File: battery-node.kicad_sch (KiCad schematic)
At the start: 16 parts, among them Q2 TK11S10N1L,LQ, U1 L99BM114-TR

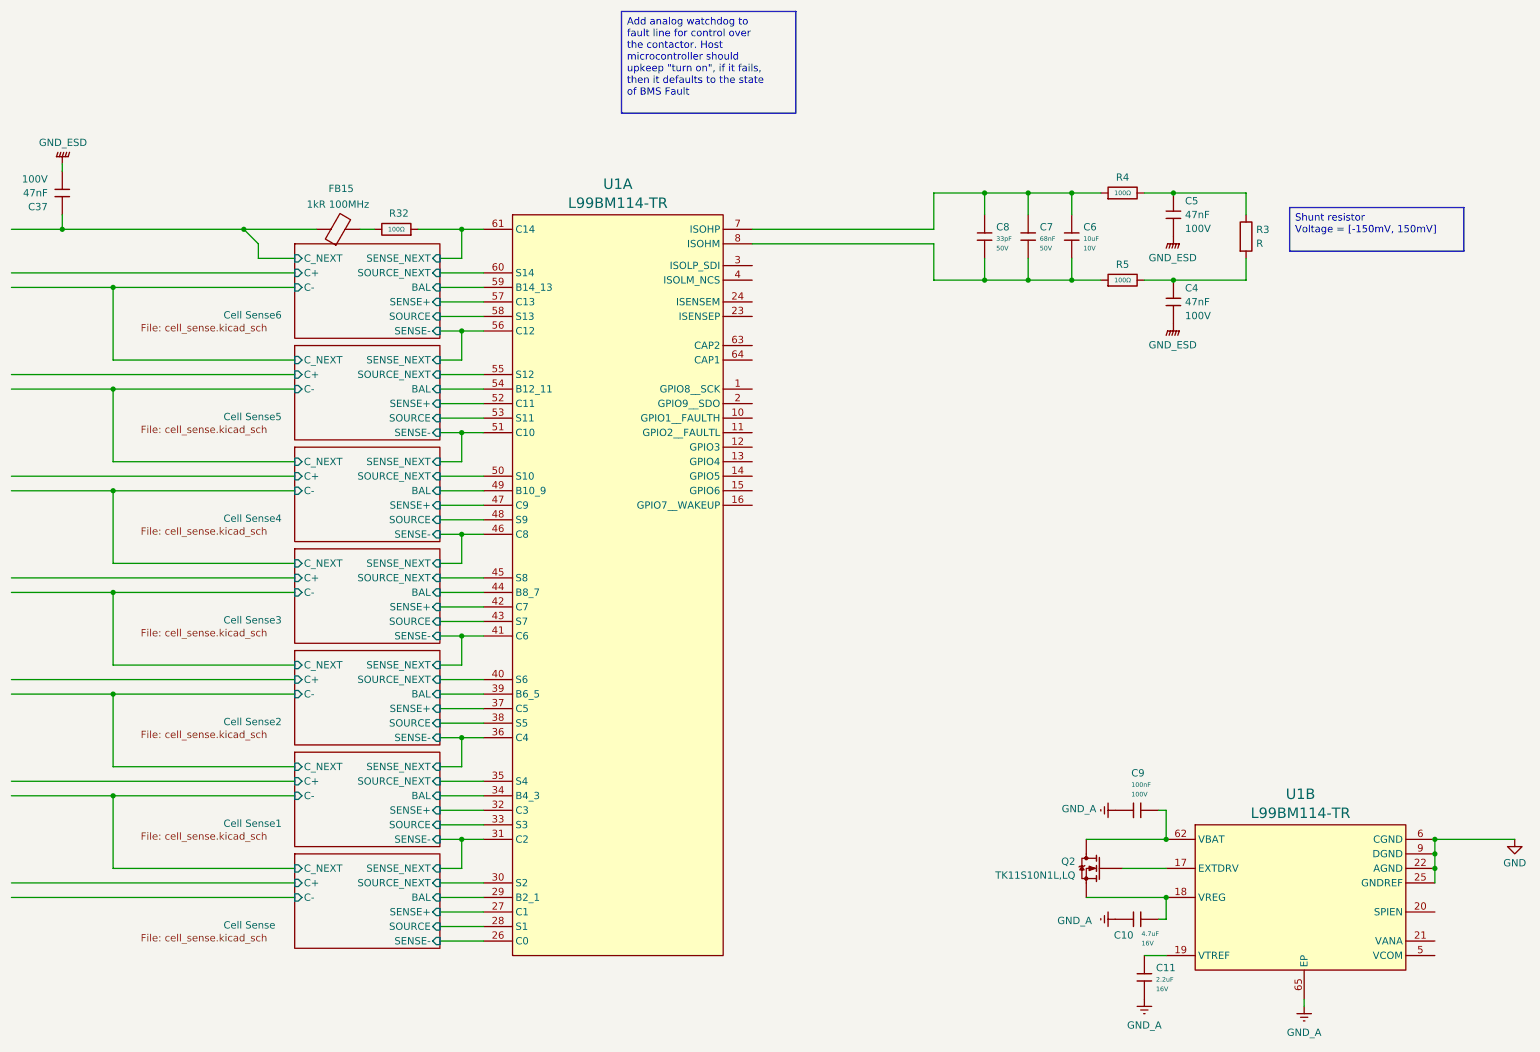
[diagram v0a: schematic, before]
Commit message: Continued work on adding subcircuits for L99BM114
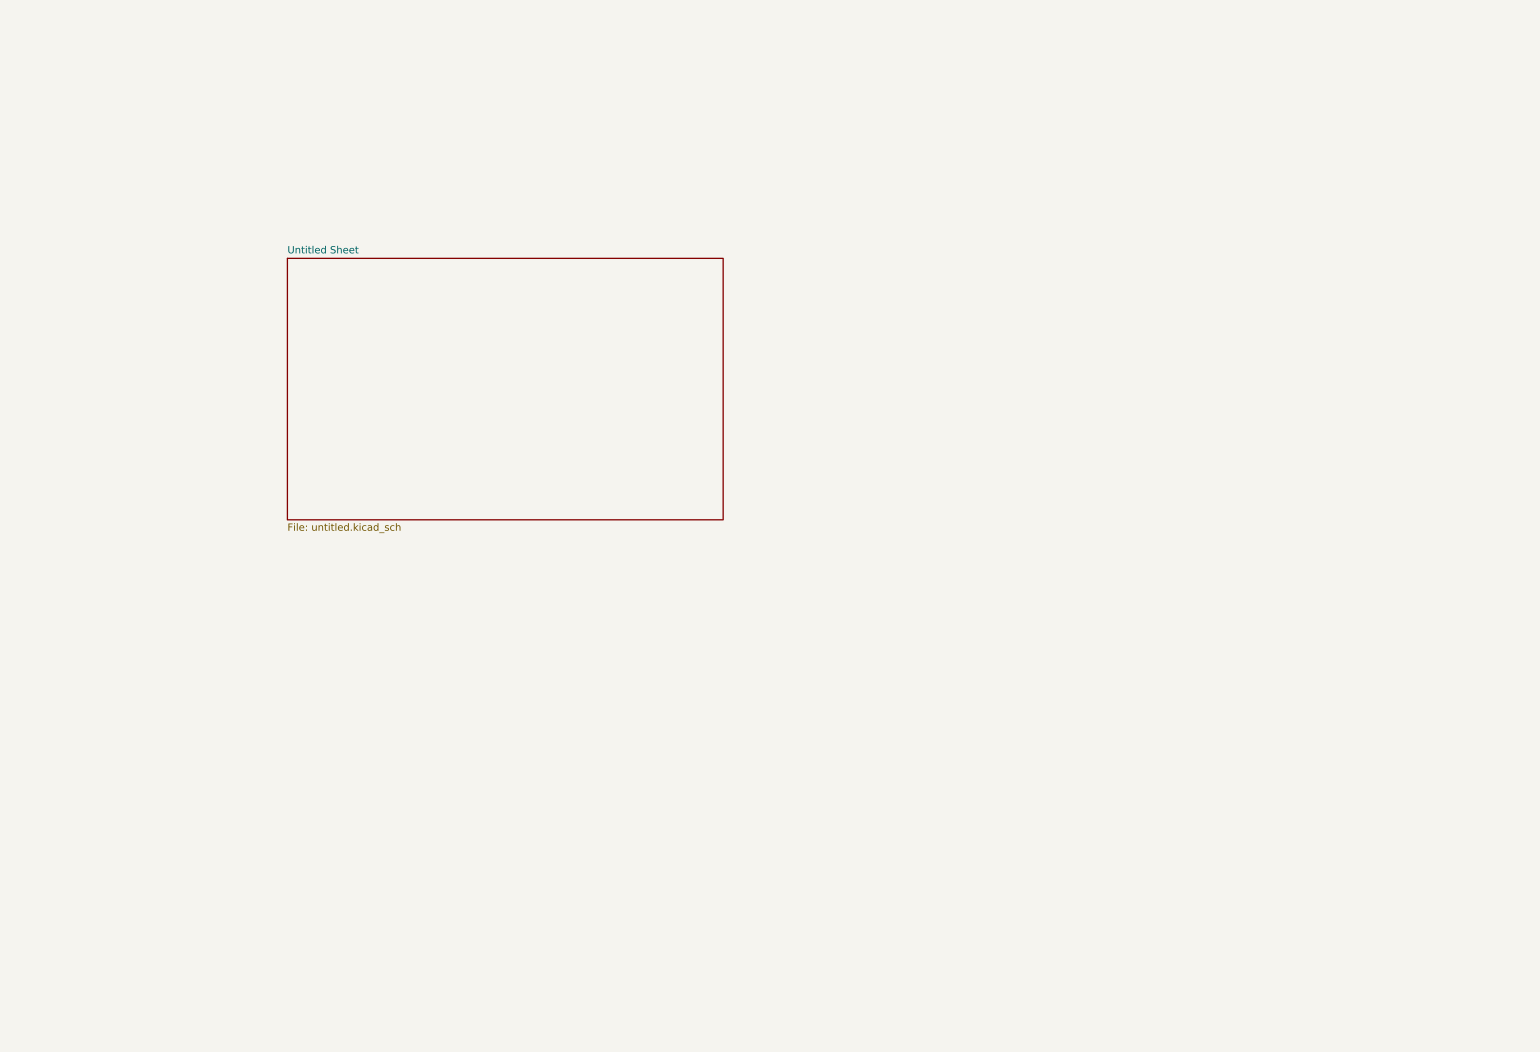
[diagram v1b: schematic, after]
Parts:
- removed C10: 4.7uF, PCM_JLCPCB:C_0603, symbol PCM_JLCPCB-Capacitors:0603,4.7uF
- removed C11: 2.2uF, PCM_JLCPCB:C_0603, symbol PCM_JLCPCB-Capacitors:0603,2.2uF
- removed C37, C4, C5: 47nF, symbol ct_lib:CC0603KRX7R0BB473
- removed C6: 10uF, PCM_JLCPCB:C_0603, symbol PCM_JLCPCB-Capacitors:0603,10uF
- removed C7: 68nF, PCM_JLCPCB:C_0603, symbol PCM_JLCPCB-Capacitors:0603,68nF
- removed C8: 33pF, PCM_JLCPCB:C_0402, symbol PCM_JLCPCB-Capacitors:0402,33pF
- removed C9: 100nF, PCM_JLCPCB:C_0805, symbol PCM_JLCPCB-Capacitors:0805,100nF
- removed FB15: 1kR 100MHz, symbol ct_lib:MPZ2012S102ATD25
- removed Q2: TK11S10N1L,LQ, symbol ct_lib:TK11S10N1L,LQ
- removed R3: R, symbol Device:R
- removed R32, R4, R5: 100Ω, PCM_JLCPCB:R_0402, symbol PCM_JLCPCB-Resistors:0402,100Ω
- removed U1: L99BM114-TR, symbol ct_lib:L99BM114-TR
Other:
- removed sheet Cell Sense
- removed sheet Cell Sense1
- removed sheet Cell Sense2
- removed sheet Cell Sense3
- removed sheet Cell Sense4
- removed sheet Cell Sense5
- removed sheet Cell Sense6
- added sheet Untitled Sheet (untitled.kicad_sch)

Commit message: gave untitled file a name
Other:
- sheet Untitled Sheet renamed BMS
- sheet BMS: file untitled.kicad_sch -> bms.kicad_sch
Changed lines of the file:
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@@
 			(color 0 0 0 0.0000)
 		)
-		(property "Sheetname" "Untitled Sheet"
+		(property "Sheetname" "BMS"
 			(at 129.54 57.7084 0)
 			(effects
@@
 			)
 		)
-		(property "Sheetfile" "untitled.kicad_sch"
+		(property "Sheetfile" "bms.kicad_sch"
 			(at 129.54 104.7246 0)
 			(effects

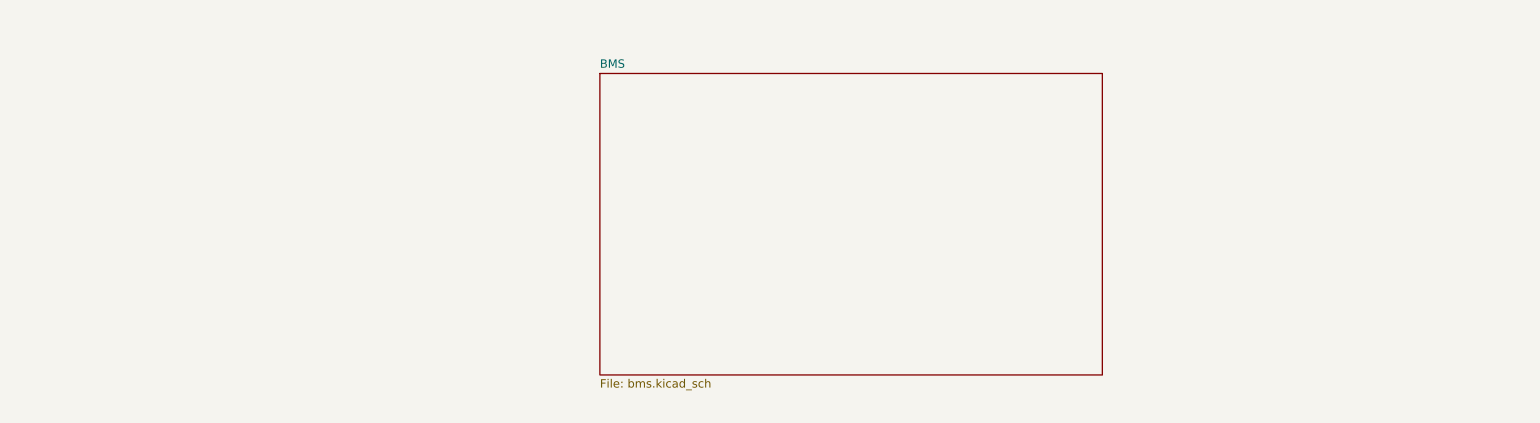
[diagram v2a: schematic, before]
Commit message: added BQ chip
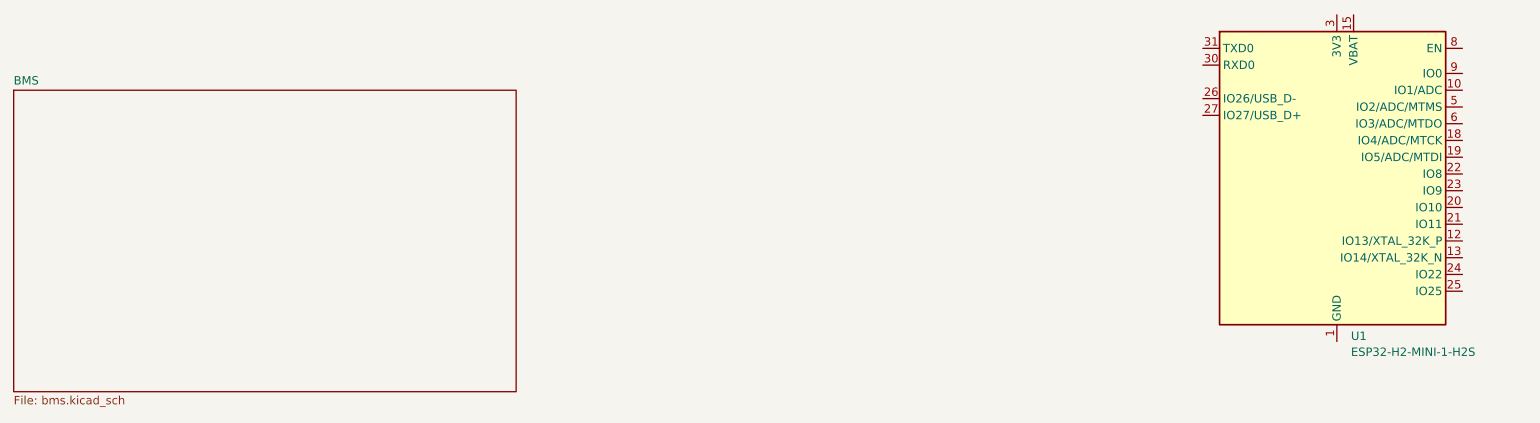
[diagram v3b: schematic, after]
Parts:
- added U1: ESP32-H2-MINI-1-H2S, symbol ct_lib:ESP32-H2-MINI-1-H2S
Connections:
- new net: U1.1 (GND), U1.11 (GND), U1.14 (GND), U1.2 (GND), U1.36 (GND), U1.37 (GND), U1.38 (GND), U1.39 (GND), U1.40 (GND), U1.41 (GND), U1.42 (GND), U1.43 (GND), U1.44 (GND), U1.45 (GND), U1.46 (GND), U1.47 (GND), U1.48 (GND), U1.49 (GND), U1.50 (GND), U1.51 (GND), U1.52 (GND), U1.53 (GND)
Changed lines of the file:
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@@
 	(generator_version "9.0")
 	(paper "B")
+	(symbol
+		(lib_id "ct_lib:ESP32-H2-MINI-1-H2S")
+		(at 241.3 82.55 0)
+		(unit 1)
+		(exclude_from_sim no)
+		(in_bom yes)
+		(on_board yes)
+		(dnp no)
+		(fields_autoplaced yes)
+		(property "Reference" "U1"
+			(at 243.4433 98.2401 0)
+			(effects
+				(font
+					(size 1.27 1.27)
+				)
+				(justify left)
+			)
+		)
+		(property "Value" "ESP32-H2-MINI-1-H2S"
+			(at 243.4433 100.6644 0)
+			(effects
+				(font
+					(size 1.27 1.27)
+				)
+				(justify left)
+			)
+		)
+		(property "Footprint" ""
+			(at 241.3 82.55 0)
+			(effects
+				(font
+					(size 1.27 1.27)
+				)
+				(hide yes)
+			)
+		)
+		(property "Datasheet" "https://documentation.espressif.com/esp32-h2-mini-1_mini-1u_datasheet_en.pdf"
+			(at 236.22 82.55 0)
+			(effects
+				(font
+					(size 1.27 1.27)
+				)
+				(hide yes)
+			)
+		)
+		(property "Description" "802.15.4, Bluetooth Bluetooth v5.3, Zigbee® Transceiver Module 2.4GHz PCB Trace Surface Mount"
+			(at 241.3 82.55 0)
+			(effects
+				(font
+					(size 1.27 1.27)
+				)
+				(hide yes)
+			)
+		)
+		(property "Manufacturer" "Espressif Systems"
+			(at 241.3 82.55 0)
+			(effects
+				(font
+					(size 1.27 1.27)
+				)
+				(hide yes)
+			)
+		)
+		(property "Part" "ESP32-H2-MINI-1-H2S"
+			(at 241.3 82.55 0)
+			(effects
+				(font
+					(size 1.27 1.27)
+				)
+				(hide yes)
+			)
+		)
+		(pin "22"
+		)
+		(pin "43"
+		)
+		(pin "21"
+		)
+		(pin "5"
+		)
+		(pin "46"
+		)
+		(pin "42"
+		)
+		(pin "53"
+		)
+		(pin "50"
+		)
+		(pin "47"
+		)
+		(pin "40"
+		)
+		(pin "48"
+		)
+		(pin "39"
+		)
+		(pin "49"
+		)
+		(pin "44"
+		)
+		(pin "51"
+		)
+		(pin "15"
+		)
+		(pin "8"
+		)
+		(pin "9"
+		)
+		(pin "10"
+		)
+		(pin "6"
+		)
+		(pin "18"
+		)
+		(pin "19"
+		)
+		(pin "41"
+		)
+		(pin "52"
+		)
+		(pin "45"
+		)
+		(pin "23"
+		)
+		(pin "20"
+		)
+		(pin "12"
+		)
+		(pin "13"
+		)
+		(pin "24"
+		)
+		(pin "25"
+		)
+		(pin "27"
+		)
+		(pin "1"
+		)
+		(pin "38"
+		)
+		(pin "3"
+		)
+		(pin "34"
+		)
+		(pin "14"
+		)
+		(pin "35"
+		)
+		(pin "30"
+		)
+		(pin "11"
+		)
+		(pin "32"
+		)
+		(pin "28"
+		)
+		(pin "4"
+		)
+		(pin "31"
+		)
+		(pin "2"
+		)
+		(pin "26"
+		)
+		(pin "36"
+		)
+		(pin "37"
+		)
+		(pin "7"
+		)
+		(pin "29"
+		)
+		(pin "17"
+		)
+		(pin "33"
+		)
+		(instances
+			(project ""
+				(path "/0531bb65-44fe-462a-8fbf-92fb22c9abe0"
+					(reference "U1")
+					(unit 1)
+				)
+			)
+		)
+	)
 	(sheet
-		(at 129.54 58.42)
+		(at 40.64 60.96)
 		(size 76.2 45.72)
 		(exclude_from_sim no)
@@
 		)
 		(property "Sheetname" "BMS"
-			(at 129.54 57.7084 0)
+			(at 40.64 60.2484 0)
 			(effects
 				(font
@@
 		)
 		(property "Sheetfile" "bms.kicad_sch"
-			(at 129.54 104.7246 0)
-			(effects
-				(font
+			(at 40.64 107.2646 0)
+			(effects
+				(font

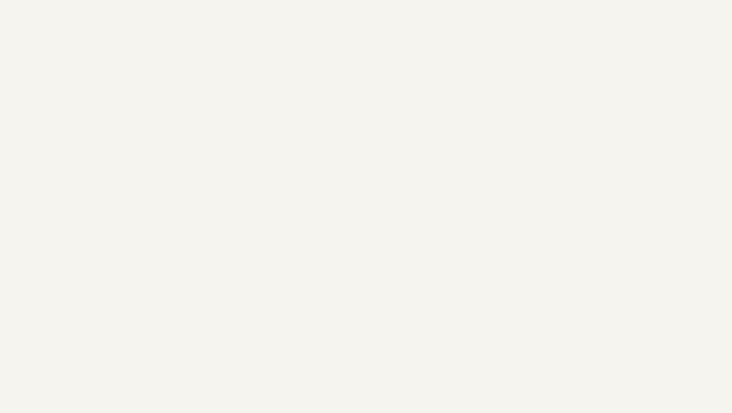
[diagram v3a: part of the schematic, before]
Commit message: Updated simulations to fix turn-off issues at negative voltages. Added power stage to BMS based on sim 5
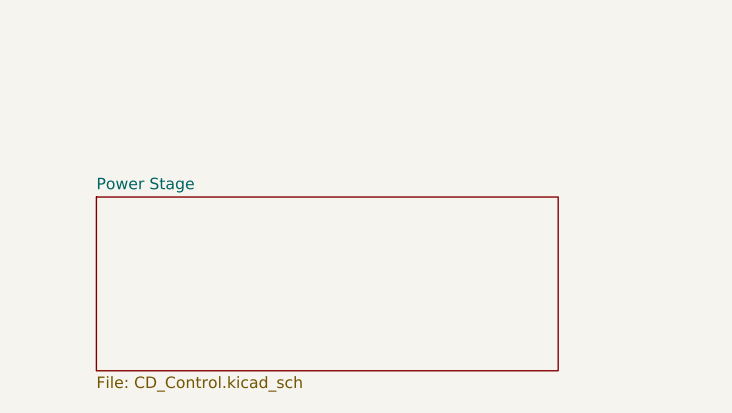
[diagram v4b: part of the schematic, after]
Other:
- added sheet Power Stage (CD_Control.kicad_sch)

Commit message: More sims, more buildout
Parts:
- added D17: NUP2105L, Package_TO_SOT_SMD:SOT-23, symbol Power_Protection:NUP2105L
- added J2, J3: Conn_01x02, symbol Connector_Generic:Conn_01x02
- added J4: Conn_01x03, symbol Connector_Generic:Conn_01x03
- added J5: Conn_01x05, symbol Connector_Generic:Conn_01x05
- added JP16: SolderJumper_2_Open, symbol Jumper:SolderJumper_2_Open
- added R37: 120Ω, PCM_JLCPCB:R_1206, symbol PCM_JLCPCB-Resistors:1206,120Ω
- added TP1: IO8, TestPoint:TestPoint_Pad_D1.0mm, symbol Connector:TestPoint
- added TP2: IO9, symbol Connector:TestPoint
- added TP3, TP4, TP5: IO25, symbol Connector:TestPoint
- added U2: ISO1050DUB, Package_SO:SOP-8_6.62x9.15mm_P2.54mm, symbol Interface_CAN_LIN:ISO1050DUB
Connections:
- net GND: now reaches U1.1 (GND), U1.11 (GND), U1.14 (GND), U1.2 (GND), U1.36 (GND), U1.37 (GND), U1.38 (GND), U1.39 (GND), U1.40 (GND), U1.41 (GND), U1.42 (GND), U1.43 (GND), U1.44 (GND), U1.45 (GND), U1.46 (GND), U1.47 (GND), U1.48 (GND), U1.49 (GND), U1.50 (GND), U1.51 (GND), U1.52 (GND), U1.53 (GND)
- net GND: now also J5.1 (Pin_1), TP5.1, U2.4 (GND1)
- net BMS/nWAKE: now reaches U1.10 (IO1/ADC)
- net at U1.17 (NC): now also U1.28 (NC), U1.29 (NC), U1.32 (NC), U1.33 (NC), U1.34 (NC), U1.35 (NC), U1.4 (NC), U1.7 (NC)
- net DBG_MTCK: now reaches U1.18 (IO4/ADC/MTCK)
- net DBG_MTCK: now also J5.3 (Pin_3)
- net DBG_MTDI: now reaches U1.19 (IO5/ADC/MTDI)
- net DBG_MTDI: now also J5.2 (Pin_2)
- net BMS/FUSE_MEAS: now reaches U1.20 (IO10)
- net BMS/AFE_SDA: now reaches U1.21 (IO11)
- net at U1.22 (IO8/BOOT0): now also TP1.1
- net at U1.23 (IO9/BOOT1): now also TP2.1
- net BMS/AFE_SDL: now reaches U1.24 (IO22)
- net at U1.25 (IO25/BOOT2): now also TP3.1
- net +3V3: now reaches U1.3 (3V3)
- net +3V3: now also TP4.1
- net at U1.30 (IO23/RXD0): now also U2.3 (TXD)
- net at U1.31 (IO24/TXD0): now also U2.2 (RXD)
- net DBG_MTMS: now reaches U1.5 (IO2/ADC/MTMS)
- net DBG_MTMS: now also J5.5 (Pin_5)
- net DBG_MTDO: now reaches U1.6 (IO3/ADC/MTDO)
- net DBG_MTDO: now also J5.4 (Pin_4)
- net BMS/ALERT: now reaches U1.9 (IO0)
- new net: D17.2 (K), J4.1 (Pin_1), R37.1, U2.7 (CANH)
- new net: JP16.2 (B), R37.2
- new net: D17.1 (K), J4.2 (Pin_2), JP16.1 (A), U2.6 (CANL)
- new net +3V3_SW: U2.1 (VCC1)
- new net BMS/CSENSE_N: J3.1 (Pin_1)
- new net BMS/CSENSE_P: J2.2 (Pin_2)
- new net GNDISO: D17.3 (A), J4.3 (Pin_3), U2.5 (GND2)
- new net Power Stage/CELLS_POSITIVE: J2.1 (Pin_1)
- new net Power Stage/PACK_POSITIVE: J3.2 (Pin_2)
- no-connect marks 0 -> 1
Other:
- sheet BMS ports: added AFE_SDA, AFE_SDL, ALERT, CHARGE_PUMP, CHG_GATE_CTRL, CSENSE_N, CSENSE_P, DSG_GATE_CTRL, FUSE_MEAS, PDSG_GATE_CTRL, nWAKE; removed none
- sheet Power Stage ports: added CELLS_NEGATIVE, CELLS_POSITIVE, CHARGE_PUMP, CHG_GATE_CTRL, DSG_GATE_CTRL, PACK_NEGATIVE, PACK_POSITIVE, PDSG_GATE_CTRL; removed none
- note added: "TXD0 will dump junk data on boot."
- note added: "mie1w0505 chip for isolated 5v/3.3v power"
- moved on the sheet: U1

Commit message: isolated comms
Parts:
- removed D17: NUP2105L, Package_TO_SOT_SMD:SOT-23, symbol Power_Protection:NUP2105L
- removed J4: Conn_01x03, symbol Connector_Generic:Conn_01x03
- removed JP16: SolderJumper_2_Open, symbol Jumper:SolderJumper_2_Open
- removed R37: 120Ω, PCM_JLCPCB:R_1206, symbol PCM_JLCPCB-Resistors:1206,120Ω
- removed U2: ISO1050DUB, Package_SO:SOP-8_6.62x9.15mm_P2.54mm, symbol Interface_CAN_LIN:ISO1050DUB
- added R41, R45: 10kΩ, PCM_JLCPCB:R_0402, symbol PCM_JLCPCB-Resistors:0402,10kΩ
- added TP12, TP13: IO25, symbol Connector:TestPoint
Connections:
- net +3V3: now also R41.2, R45.2
- net ISOLATED_COMMS/CAN_RX: now reaches U1.31 (IO24/TXD0)
- net ISOLATED_COMMS/CAN_TX: now reaches U1.30 (IO23/RXD0)
- net ISOLATED_COMMS/EN_ISO_PWR: now reaches U1.12 (IO13/XTAL_32K_P)
- net AFE/AFE_SDA renamed AFE/SDA
- net AFE/SDA: now also R41.1, TP12.1
- net AFE/AFE_SDL renamed AFE/SDL
- net AFE/SDL: now also R45.1, TP13.1
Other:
- sheet BMS renamed AFE
- sheet Power Stage renamed CHARGE_DISCHARGE_CONTROL
- added sheet ISOLATED_COMMS (CAN.kicad_sch)
- sheet AFE ports: added SDA, SDL; removed AFE_SDA, AFE_SDL
- note added: "Make power stage optional on second board Add spot to switch over between pack on 2nd board and pack onboard (pin)"
- note added: "Programming Header"
- note added: "mie1w0505 chip for isolated 5v/3.3v power? Maybe some other topology. TI has some good 2-part chips for isolated power"
- note removed: "mie1w0505 chip for isolated 5v/3.3v power"
- moved on the sheet: J5

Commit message: 10.0
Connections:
- net ISOLATED_COMMS/USB_nINT: now reaches U1.13 (IO14/XTAL_32K_N)
- net ISOLATED_COMMS/USB_D-: now reaches U1.26 (IO26/USB_D-)
- net ISOLATED_COMMS/USB_D+: now reaches U1.27 (IO27/USB_D+)
- net ISOLATED_COMMS/EN_ISO_PWR renamed ISOLATED_COMMS/nEN_ISO_PWR
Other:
- sheet ISOLATED_COMMS ports: added USB_D+, USB_D-, USB_nINT, nEN_ISO_PWR; removed EN_ISO_PWR
- note added: "interrupt"

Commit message: comms updates
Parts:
- R41: Price 0.004USD -> 0.005USD; Stock 24372091 -> 4191623
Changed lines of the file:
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@@
 	)
 	(symbol
+		(lib_name "0402,10kΩ_1")
 		(lib_id "PCM_JLCPCB-Resistors:0402,10kΩ")
 		(at 157.48 140.97 0)
@@
 			)
 		)
-		(property "Description" "62.5mW Thick Film Resistors 50V ±100ppm/°C ±1% 10kΩ 0402 Chip Resistor - Surface Mount ROHS"
+		(property "Description" "-55°C~+155°C 10kΩ 50V 62.5mW Thick Film Resistor ±1% ±100ppm/°C 0402 Chip Resistor - Surface Mount ROHS"
 			(at 157.48 140.97 0)
 			(hide yes)
@@
 			)
 		)
-		(property "Stock" "24372091"
+		(property "Stock" "4191623"
 			(at 157.48 140.97 0)
 			(hide yes)
@@
 			)
 		)
-		(property "Price" "0.004USD"
+		(property "Price" "0.005USD"
 			(at 157.48 140.97 0)
 			(hide yes)
